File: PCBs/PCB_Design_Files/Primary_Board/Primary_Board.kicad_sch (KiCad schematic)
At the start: 6 parts, among them J1 Conn_FFC_8pin, J2 Conn_01x08_Pin

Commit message: added 3rd order filter
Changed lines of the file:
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@@
 	)
 	(sheet
-		(at 86.36 46.99)
-		(size 24.13 27.94)
+		(at 81.28 46.99)
+		(size 29.21 27.94)
 		(exclude_from_sim no)
 		(in_bom yes)
@@
 		)
 		(property "Sheetname" "AFE"
-			(at 86.36 46.2784 0)
+			(at 81.28 46.2784 0)
 			(effects
 				(font
@@
 		)
 		(property "Sheetfile" "AFE.kicad_sch"
-			(at 86.36 75.5146 0)
+			(at 81.28 75.5146 0)
 			(effects
 				(font
@@
 		)
 		(pin "V_bandgap" input
-			(at 86.36 55.88 180)
+			(at 81.28 55.88 180)
 			(effects
 				(font

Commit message: added bypass
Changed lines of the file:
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@@
 	)
 	(sheet
-		(at 81.28 46.99)
-		(size 29.21 27.94)
+		(at 86.36 46.99)
+		(size 24.13 27.94)
 		(exclude_from_sim no)
 		(in_bom yes)
@@
 		)
 		(property "Sheetname" "AFE"
-			(at 81.28 46.2784 0)
+			(at 86.36 46.2784 0)
 			(effects
 				(font
@@
 		)
 		(property "Sheetfile" "AFE.kicad_sch"
-			(at 81.28 75.5146 0)
+			(at 86.36 75.5146 0)
 			(effects
 				(font
@@
 		)
 		(pin "V_bandgap" input
-			(at 81.28 55.88 180)
+			(at 86.36 55.88 180)
 			(effects
 				(font

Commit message: updated AFE pcb
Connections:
- net V_bandgap: now also J1.7, J2.7 (Pin_7); no longer J1.6, J2.6 (Pin_6)
- net V_ptat: now also J1.6, J2.6 (Pin_6); no longer J1.7, J2.7 (Pin_7)
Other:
- note removed: "Have unused opamp, could use it as a buffer for ptat signal so it doesn't go to waste"
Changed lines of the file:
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@@
-		)
-	)
-	(text "Have unused opamp, could use it\nas a buffer for ptat signal so it\ndoesn't go to waste"
-		(exclude_from_sim no)
-		(at 97.79 82.55 0)
-		(effects
-			(font
-				(size 1.27 1.27)
-			)
 		)
 	)
@@
 	(wire
 		(pts
+			(xy 59.69 125.73) (xy 59.69 124.46)
+		)
+		(stroke
+			(width 0)
+			(type default)
+		)
+	)
+	(wire
+		(pts
+			(xy 58.42 106.68) (xy 58.42 109.22)
+		)
+		(stroke
+			(width 0)
+			(type default)
+		)
+	)
+	(wire
+		(pts
+			(xy 43.18 114.3) (xy 59.69 114.3)
+		)
+		(stroke
+			(width 0)
+			(type default)
+		)
+	)
+	(wire
+		(pts
+			(xy 43.18 111.76) (xy 59.69 111.76)
+		)
+		(stroke
+			(width 0)
+			(type default)
+		)
+	)
+	(wire
+		(pts
+			(xy 110.49 71.12) (xy 125.73 71.12)
+		)
+		(stroke
+			(width 0)
+			(type default)
+		)
+	)
+	(wire
+		(pts
+			(xy 110.49 52.07) (xy 125.73 52.07)
+		)
+		(stroke
+			(width 0)
+			(type default)
+		)
+	)
+	(wire
+		(pts
+			(xy 55.88 106.68) (xy 58.42 106.68)
+		)
+		(stroke
+			(width 0)
+			(type default)
+		)
+	)
+	(wire
+		(pts
+			(xy 55.88 106.68) (xy 55.88 107.95)
+		)
+		(stroke
+			(width 0)
+			(type default)
+		)
+	)
+	(wire
+		(pts
+			(xy 44.45 109.22) (xy 44.45 106.68)
+		)
+		(stroke
+			(width 0)
+			(type default)
+		)
+	)
+	(wire
+		(pts
+			(xy 59.69 132.08) (xy 50.8 132.08)
+		)
+		(stroke
+			(width 0)
+			(type default)
+		)
+	)
+	(wire
+		(pts
+			(xy 59.69 115.57) (xy 59.69 116.84)
+		)
+		(stroke
+			(width 0)
+			(type default)
+		)
+	)
+	(wire
+		(pts
+			(xy 43.18 125.73) (xy 43.18 124.46)
+		)
+		(stroke
+			(width 0)
+			(type default)
+		)
+	)
+	(wire
+		(pts
+			(xy 44.45 106.68) (xy 55.88 106.68)
+		)
+		(stroke
+			(width 0)
+			(type default)
+		)
+	)
+	(wire
+		(pts
+			(xy 43.18 127) (xy 43.18 132.08)
+		)
+		(stroke
+			(width 0)
+			(type default)
+		)
+	)
+	(wire
+		(pts
+			(xy 58.42 109.22) (xy 59.69 109.22)
+		)
+		(stroke
+			(width 0)
+			(type default)
+		)
+	)
+	(wire
+		(pts
+			(xy 43.18 125.73) (xy 50.8 125.73)
+		)
+		(stroke
+			(width 0)
+			(type default)
+		)
+	)
+	(wire
+		(pts
+			(xy 43.18 115.57) (xy 57.1488 115.57)
+		)
+		(stroke
+			(width 0)
+			(type default)
+		)
+	)
+	(wire
+		(pts
+			(xy 50.8 125.73) (xy 59.69 125.73)
+		)
+		(stroke
+			(width 0)
+			(type default)
+		)
+	)
+	(wire
+		(pts
+			(xy 43.18 121.92) (xy 59.69 121.92)
+		)
+		(stroke
+			(width 0)
+			(type default)
+		)
+	)
+	(wire
+		(pts
 			(xy 110.49 58.42) (xy 125.73 58.42)
 		)
@@
 	(wire
 		(pts
-			(xy 59.69 125.73) (xy 59.69 124.46)
-		)
-		(stroke
-			(width 0)
-			(type default)
-		)
-	)
-	(wire
-		(pts
-			(xy 58.42 106.68) (xy 58.42 109.22)
-		)
-		(stroke
-			(width 0)
-			(type default)
-		)
-	)
-	(wire
-		(pts
-			(xy 43.18 114.3) (xy 59.69 114.3)
-		)
-		(stroke
-			(width 0)
-			(type default)
-		)
-	)
-	(wire
-		(pts
-			(xy 43.18 111.76) (xy 59.69 111.76)
-		)
-		(stroke
-			(width 0)
-			(type default)
-		)
-	)
-	(wire
-		(pts
-			(xy 110.49 71.12) (xy 125.73 71.12)
-		)
-		(stroke
-			(width 0)
-			(type default)
-		)
-	)
-	(wire
-		(pts
-			(xy 110.49 52.07) (xy 125.73 52.07)
-		)
-		(stroke
-			(width 0)
-			(type default)
-		)
-	)
-	(wire
-		(pts
-			(xy 55.88 106.68) (xy 58.42 106.68)
-		)
-		(stroke
-			(width 0)
-			(type default)
-		)
-	)
-	(wire
-		(pts
-			(xy 55.88 106.68) (xy 55.88 107.95)
-		)
-		(stroke
-			(width 0)
-			(type default)
-		)
-	)
-	(wire
-		(pts
-			(xy 44.45 109.22) (xy 44.45 106.68)
-		)
-		(stroke
-			(width 0)
-			(type default)
-		)
-	)
-	(wire
-		(pts
-			(xy 59.69 132.08) (xy 50.8 132.08)
-		)
-		(stroke
-			(width 0)
-			(type default)
-		)
-	)
-	(wire
-		(pts
-			(xy 59.69 115.57) (xy 59.69 116.84)
-		)
-		(stroke
-			(width 0)
-			(type default)
-		)
-	)
-	(wire
-		(pts
-			(xy 43.18 125.73) (xy 43.18 124.46)
-		)
-		(stroke
-			(width 0)
-			(type default)
-		)
-	)
-	(wire
-		(pts
-			(xy 44.45 106.68) (xy 55.88 106.68)
-		)
-		(stroke
-			(width 0)
-			(type default)
-		)
-	)
-	(wire
-		(pts
-			(xy 43.18 127) (xy 43.18 132.08)
-		)
-		(stroke
-			(width 0)
-			(type default)
-		)
-	)
-	(wire
-		(pts
-			(xy 58.42 109.22) (xy 59.69 109.22)
-		)
-		(stroke
-			(width 0)
-			(type default)
-		)
-	)
-	(wire
-		(pts
-			(xy 43.18 125.73) (xy 50.8 125.73)
-		)
-		(stroke
-			(width 0)
-			(type default)
-		)
-	)
-	(wire
-		(pts
-			(xy 43.18 115.57) (xy 57.1488 115.57)
-		)
-		(stroke
-			(width 0)
-			(type default)
-		)
-	)
-	(wire
-		(pts
-			(xy 50.8 125.73) (xy 59.69 125.73)
-		)
-		(stroke
-			(width 0)
-			(type default)
-		)
-	)
-	(wire
-		(pts
-			(xy 43.18 121.92) (xy 59.69 121.92)
-		)
-		(stroke
-			(width 0)
-			(type default)
-		)
-	)
-	(wire
-		(pts
 			(xy 59.69 127) (xy 59.69 132.08)
 		)
@@
 			(width 0)
 			(type default)
-		)
-	)
-	(label "V_bandgap"
-		(at 44.45 114.3 0)
-		(effects
-			(font
-				(size 1.27 1.27)
-			)
-			(justify left bottom)
 		)
 	)
@@
 		)
 	)
+	(label "V_ptat"
+		(at 44.45 114.3 0)
+		(effects
+			(font
+				(size 1.27 1.27)
+			)
+			(justify left bottom)
+		)
+	)
 	(label "PWM_IR"
 		(at 44.45 119.38 0)
@@
 		)
 	)
-	(label "V_ptat"
+	(label "V_bandgap"
 		(at 44.45 111.76 0)
 		(effects
@@
 	(sheet
 		(at 172.72 46.99)
-		(size 22.86 21.59)
+		(size 31.75 27.94)
 		(exclude_from_sim no)
 		(in_bom yes)
@@
 		)
 		(property "Sheetfile" "MCU_Display.kicad_sch"
-			(at 172.72 69.1646 0)
-			(effects
-				(font
+			(at 172.72 75.5146 0)
+			(effects
+				(font

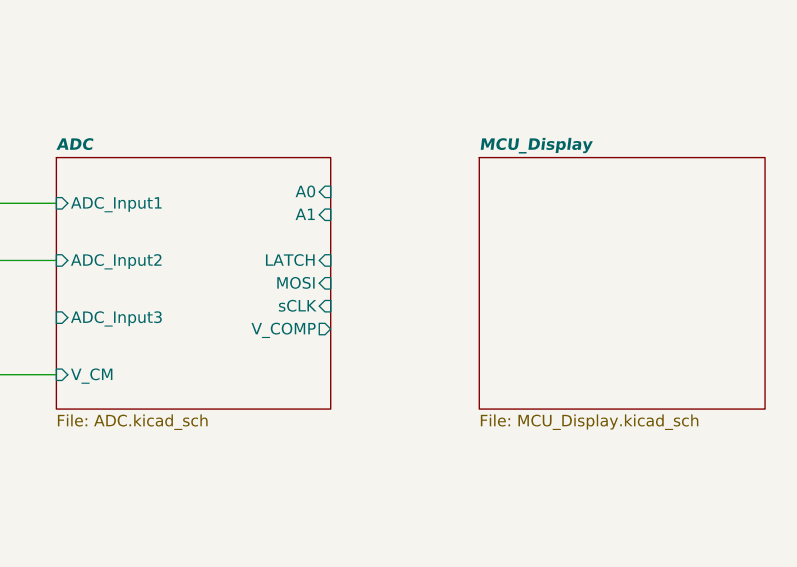
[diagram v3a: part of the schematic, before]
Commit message: Added Voltage Search DAC
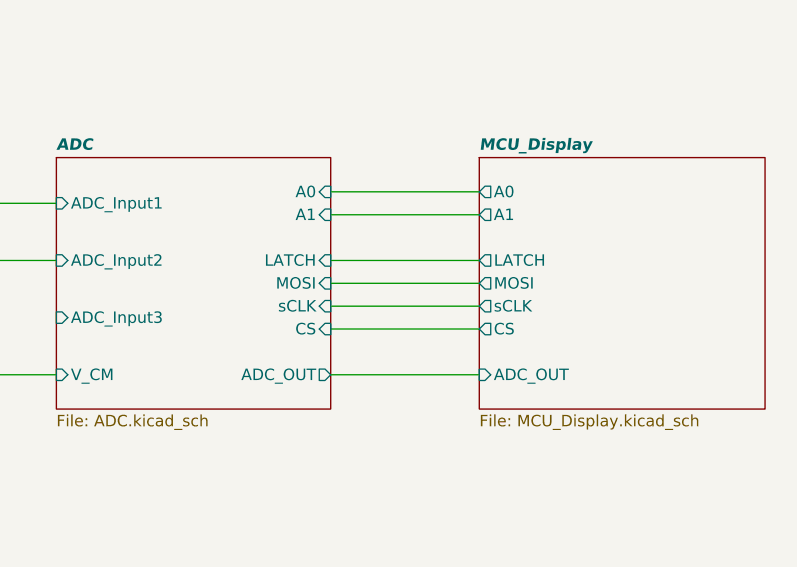
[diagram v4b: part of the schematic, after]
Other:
- sheet ADC ports: added ADC_OUT, CS; removed V_COMP
- sheet MCU_Display ports: added A0, A1, ADC_OUT, CS, LATCH, MOSI, sCLK; removed none
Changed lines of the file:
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@@
+	(wire
+		(pts
+			(xy 156.21 53.34) (xy 172.72 53.34)
+		)
+		(stroke
+			(width 0)
+			(type default)
+		)
+	)
+	(wire
+		(pts
+			(xy 156.21 63.5) (xy 172.72 63.5)
+		)
+		(stroke
+			(width 0)
+			(type default)
+		)
+	)
 	(wire
 		(pts
@@
 	(wire
 		(pts
+			(xy 156.21 58.42) (xy 172.72 58.42)
+		)
+		(stroke
+			(width 0)
+			(type default)
+		)
+	)
+	(wire
+		(pts
 			(xy 110.49 71.12) (xy 125.73 71.12)
 		)
@@
 	(wire
 		(pts
+			(xy 156.21 71.12) (xy 172.72 71.12)
+		)
+		(stroke
+			(width 0)
+			(type default)
+		)
+	)
+	(wire
+		(pts
 			(xy 110.49 52.07) (xy 125.73 52.07)
 		)
@@
 	(wire
 		(pts
+			(xy 156.21 60.96) (xy 172.72 60.96)
+		)
+		(stroke
+			(width 0)
+			(type default)
+		)
+	)
+	(wire
+		(pts
 			(xy 59.69 115.57) (xy 59.69 116.84)
 		)
@@
 	(wire
 		(pts
+			(xy 156.21 50.8) (xy 172.72 50.8)
+		)
+		(stroke
+			(width 0)
+			(type default)
+		)
+	)
+	(wire
+		(pts
 			(xy 43.18 121.92) (xy 59.69 121.92)
 		)
@@
 		(pts
 			(xy 59.69 127) (xy 59.69 132.08)
+		)
+		(stroke
+			(width 0)
+			(type default)
+		)
+	)
+	(wire
+		(pts
+			(xy 156.21 66.04) (xy 172.72 66.04)
 		)
 		(stroke
@@
 			)
 		)
-		(pin "V_COMP" output
+		(pin "CS" input
 			(at 156.21 66.04 0)
+			(effects
+				(font
+					(size 1.27 1.27)
+				)
+				(justify right)
+			)
+		)
+		(pin "ADC_OUT" output
+			(at 156.21 71.12 0)
 			(effects
 				(font
@@
 			)
 		)
+		(pin "A0" output
+			(at 172.72 50.8 180)
+			(effects
+				(font
+					(size 1.27 1.27)
+				)
+				(justify left)
+			)
+		)
+		(pin "A1" output
+			(at 172.72 53.34 180)
+			(effects
+				(font
+					(size 1.27 1.27)
+				)
+				(justify left)
+			)
+		)
+		(pin "CS" output
+			(at 172.72 66.04 180)
+			(effects
+				(font
+					(size 1.27 1.27)
+				)
+				(justify left)
+			)
+		)
+		(pin "LATCH" output
+			(at 172.72 58.42 180)
+			(effects
+				(font
+					(size 1.27 1.27)
+				)
+				(justify left)
+			)
+		)
+		(pin "MOSI" output
+			(at 172.72 60.96 180)
+			(effects
+				(font
+					(size 1.27 1.27)
+				)
+				(justify left)
+			)
+		)
+		(pin "sCLK" output
+			(at 172.72 63.5 180)
+			(effects
+				(font
+					(size 1.27 1.27)
+				)
+				(justify left)
+			)
+		)
+		(pin "ADC_OUT" input
+			(at 172.72 71.12 180)
+			(effects
+				(font
+					(size 1.27 1.27)
+				)
+				(justify left)
+			)
+		)

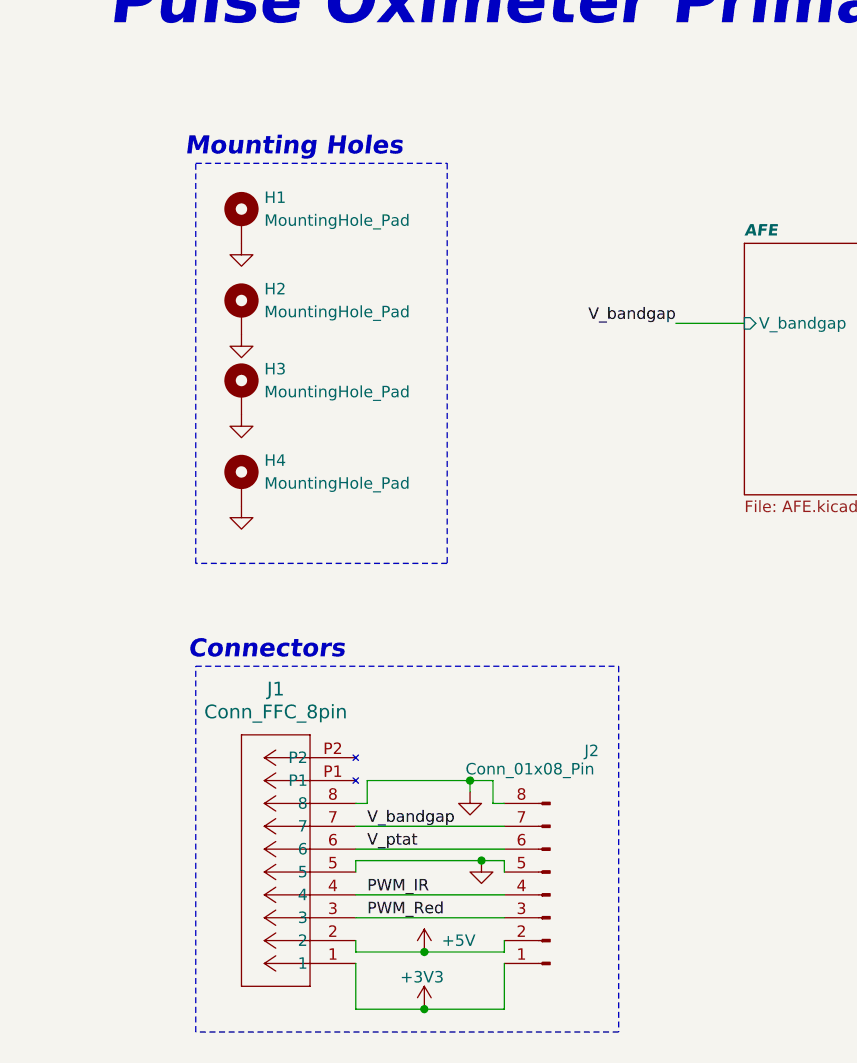
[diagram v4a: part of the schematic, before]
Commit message: updated esp library, primary board connector
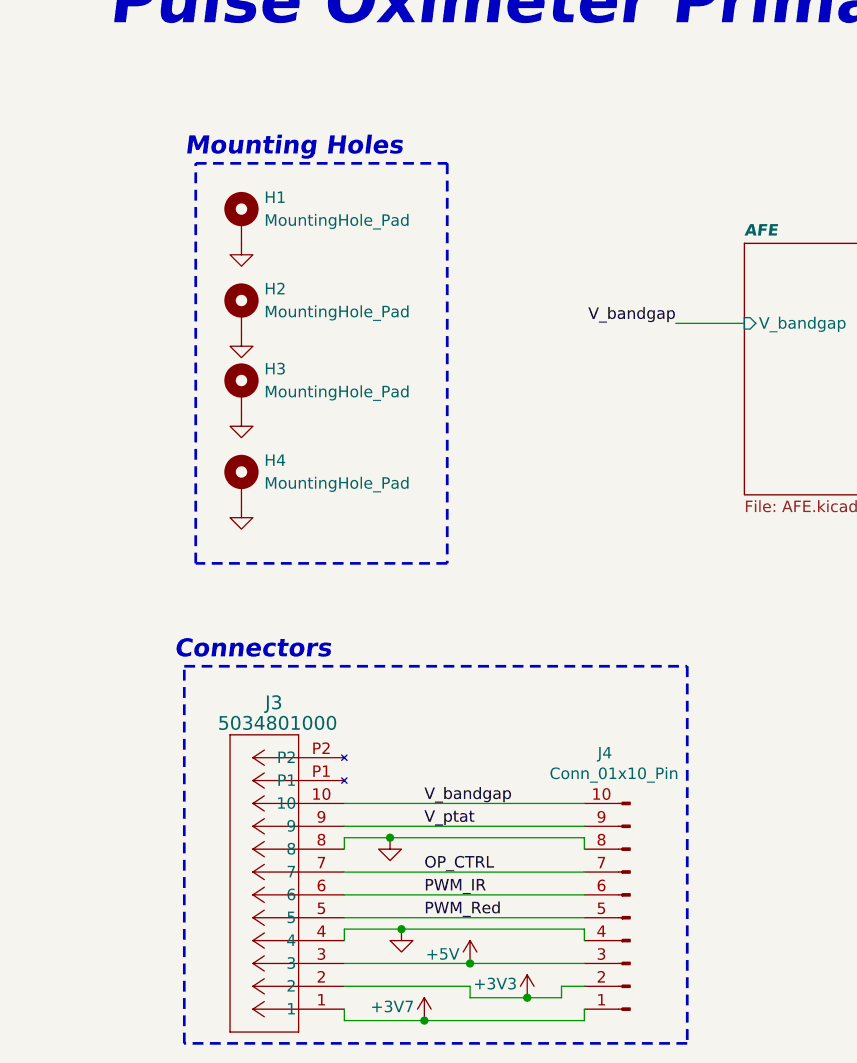
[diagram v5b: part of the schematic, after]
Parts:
- removed J1: Conn_FFC_8pin, Project Footprints:Conn_FFC_8pin, symbol Project_Symbols:Conn_FFC_8pin
- removed J2: Conn_01x08_Pin, Connector_PinHeader_2.54mm:PinHeader_1x08_P2.54mm_Vertical, symbol Connector:Conn_01x08_Pin
- added J3: 5034801000, Project Footprints:Conn_FFC_10pin, symbol project_symbols:5034801000
- added J4: Conn_01x10_Pin, Connector_PinHeader_2.54mm:PinHeader_1x10_P2.54mm_Vertical, symbol Connector:Conn_01x10_Pin
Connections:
- net +3V3: now also J3.2, J4.2 (Pin_2)
- net +5V: now also J3.3, J4.3 (Pin_3)
- net GND: now also J3.4, J3.8, J4.4 (Pin_4), J4.8 (Pin_8)
- net PWM_IR: now also J3.6, J4.6 (Pin_6)
- net PWM_Red: now also J3.5, J4.5 (Pin_5)
- net V_bandgap: now also J3.10, J4.10 (Pin_10)
- net V_ptat: now also J3.9, J4.9 (Pin_9)
- new net +3V7: J3.1, J4.1 (Pin_1)
- new net OP_CTRL: J3.7, J4.7 (Pin_7)
